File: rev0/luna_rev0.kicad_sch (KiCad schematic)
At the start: 19 parts, among them J1 USB_C_Receptacle_USB2.0, J2 USB_C_Receptacle_USB2.0, J3 USB_A, J4 USB_C_Receptacle_USB2.0, J7 PMOD_A, J8 PMOD_B, SW1 BTN_DFU, SW2 BTN_RESET, SW3 BTN_BTN

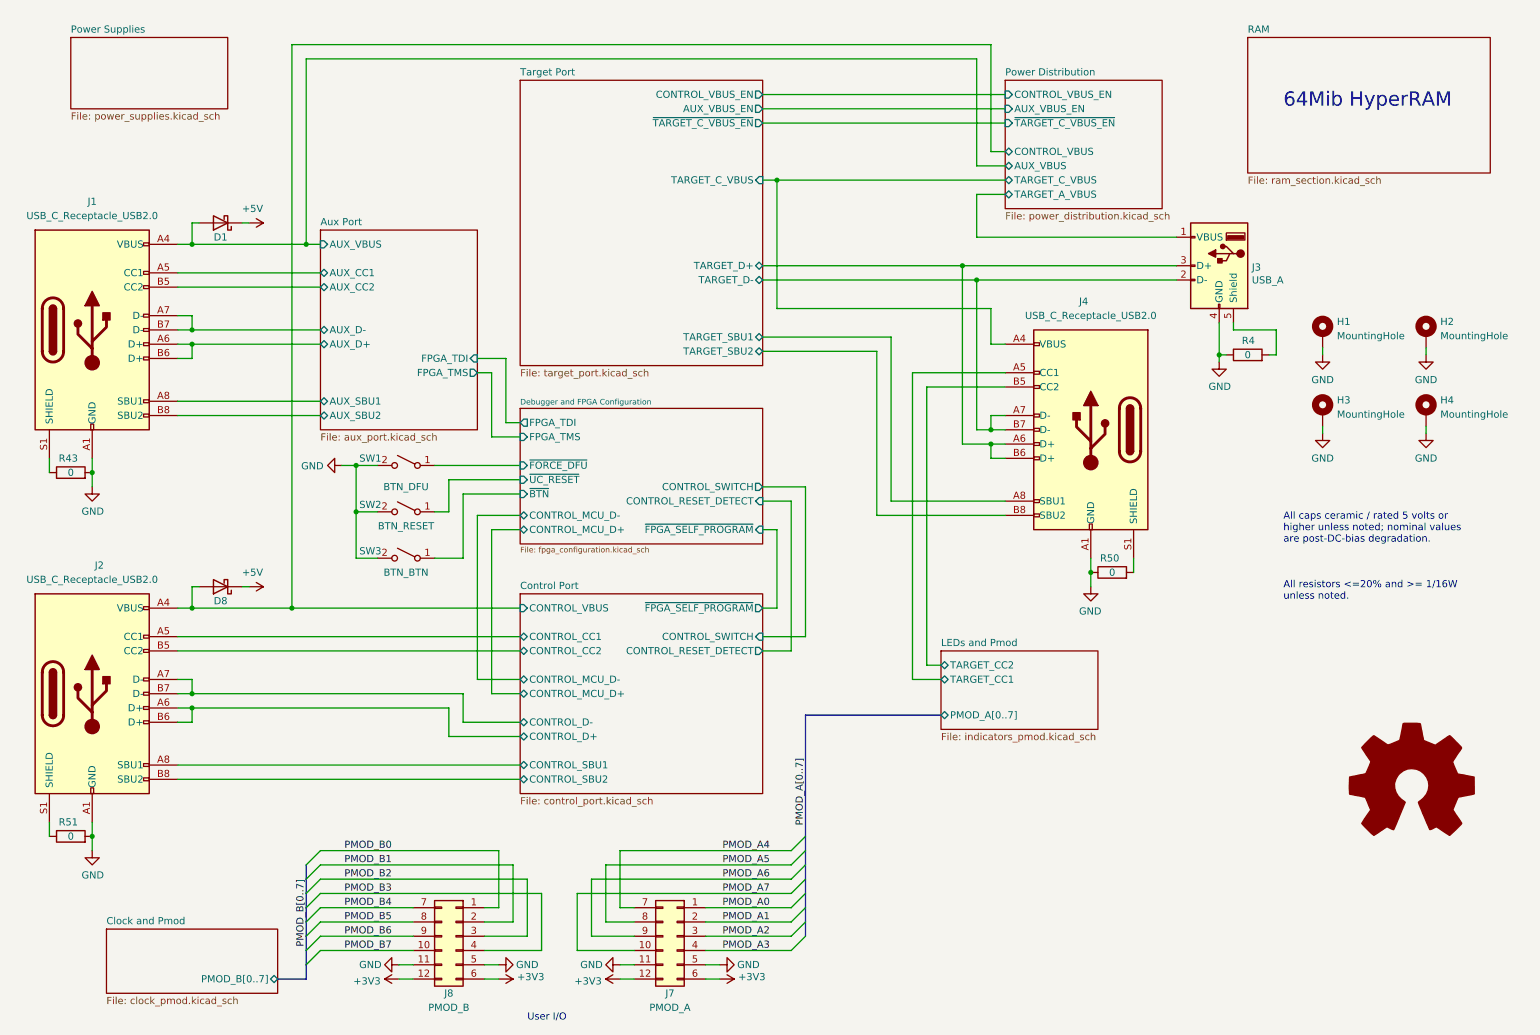
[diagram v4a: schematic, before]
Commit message: hardware: replace power input diodes
- provide input selection capability with FETs
- reduce reverse leakage current
- provide overvoltage protection
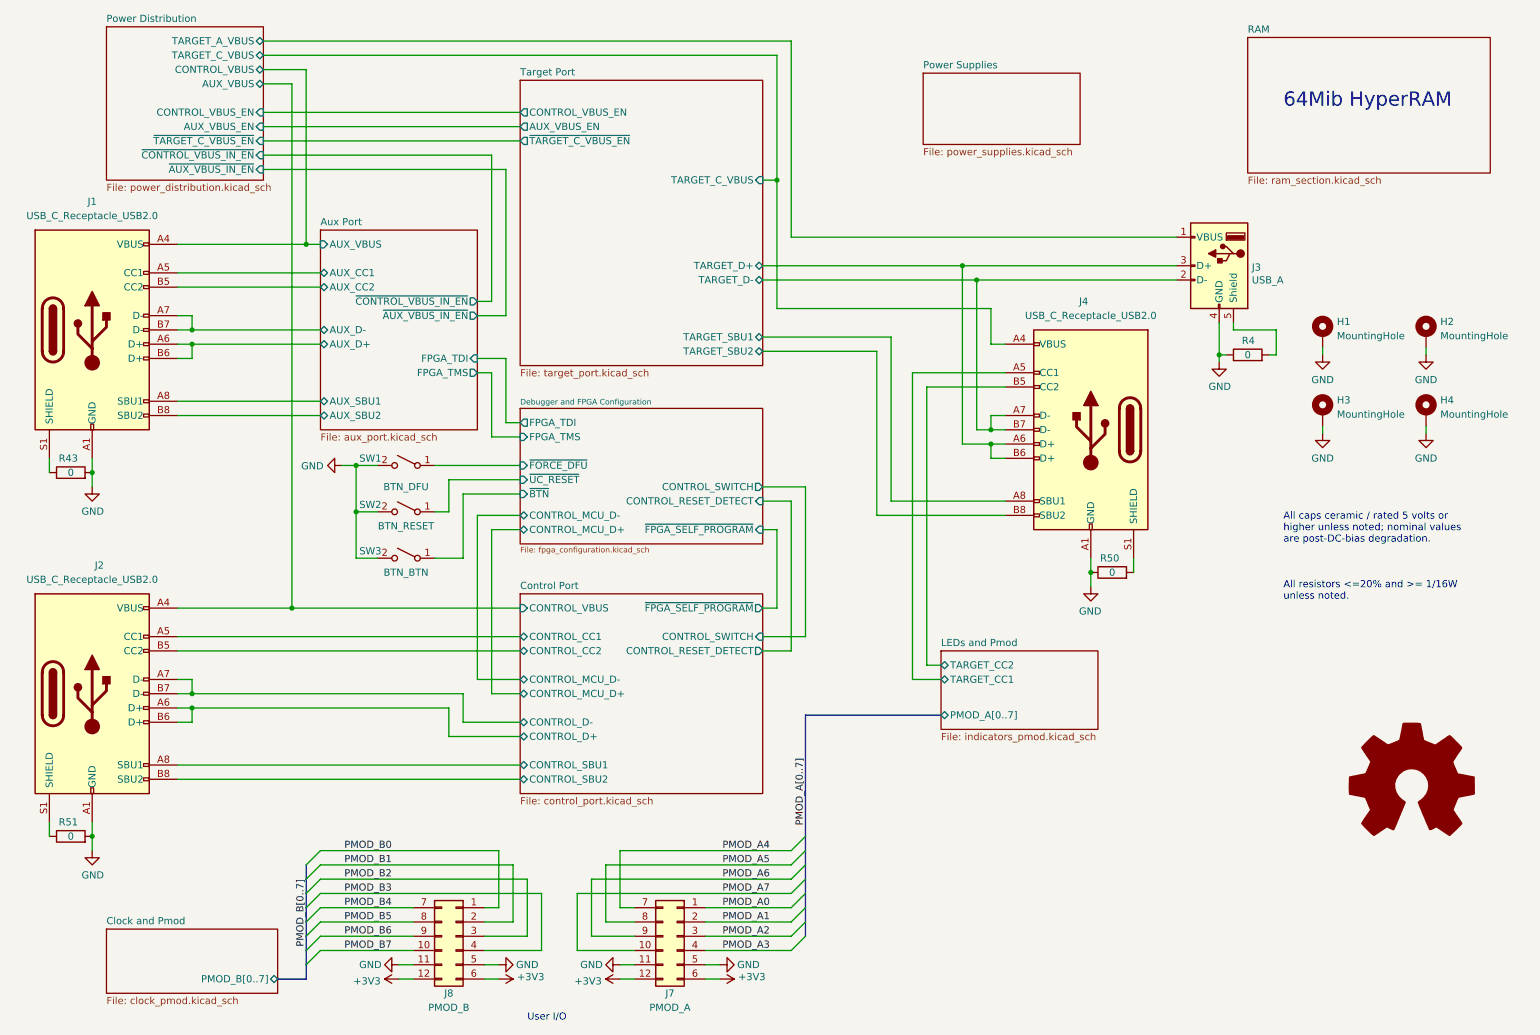
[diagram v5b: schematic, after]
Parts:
- removed D1, D8: PMEG3050BEP,115, luna:SOD128, symbol Device:D_Schottky
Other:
- sheet Aux Port ports: added ~{AUX_VBUS_IN_EN}, ~{CONTROL_VBUS_IN_EN}; removed none
- sheet Power Distribution ports: added ~{AUX_VBUS_IN_EN}, ~{CONTROL_VBUS_IN_EN}; removed none

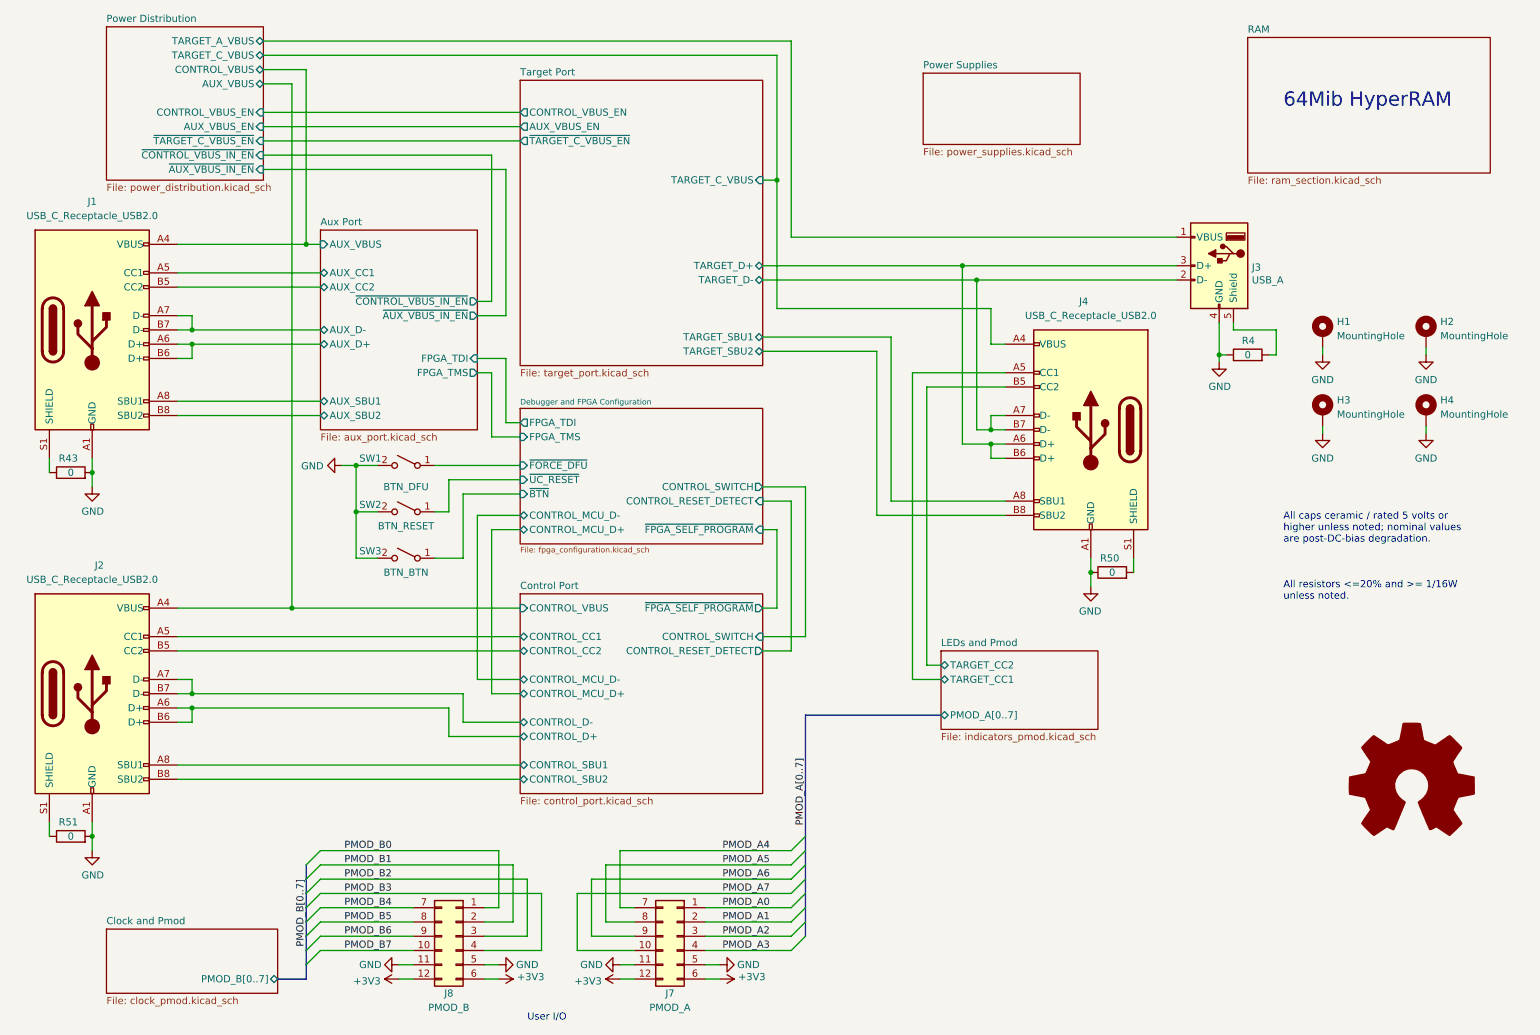
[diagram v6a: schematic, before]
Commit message: hardware: add VBUS voltage and current monitoring
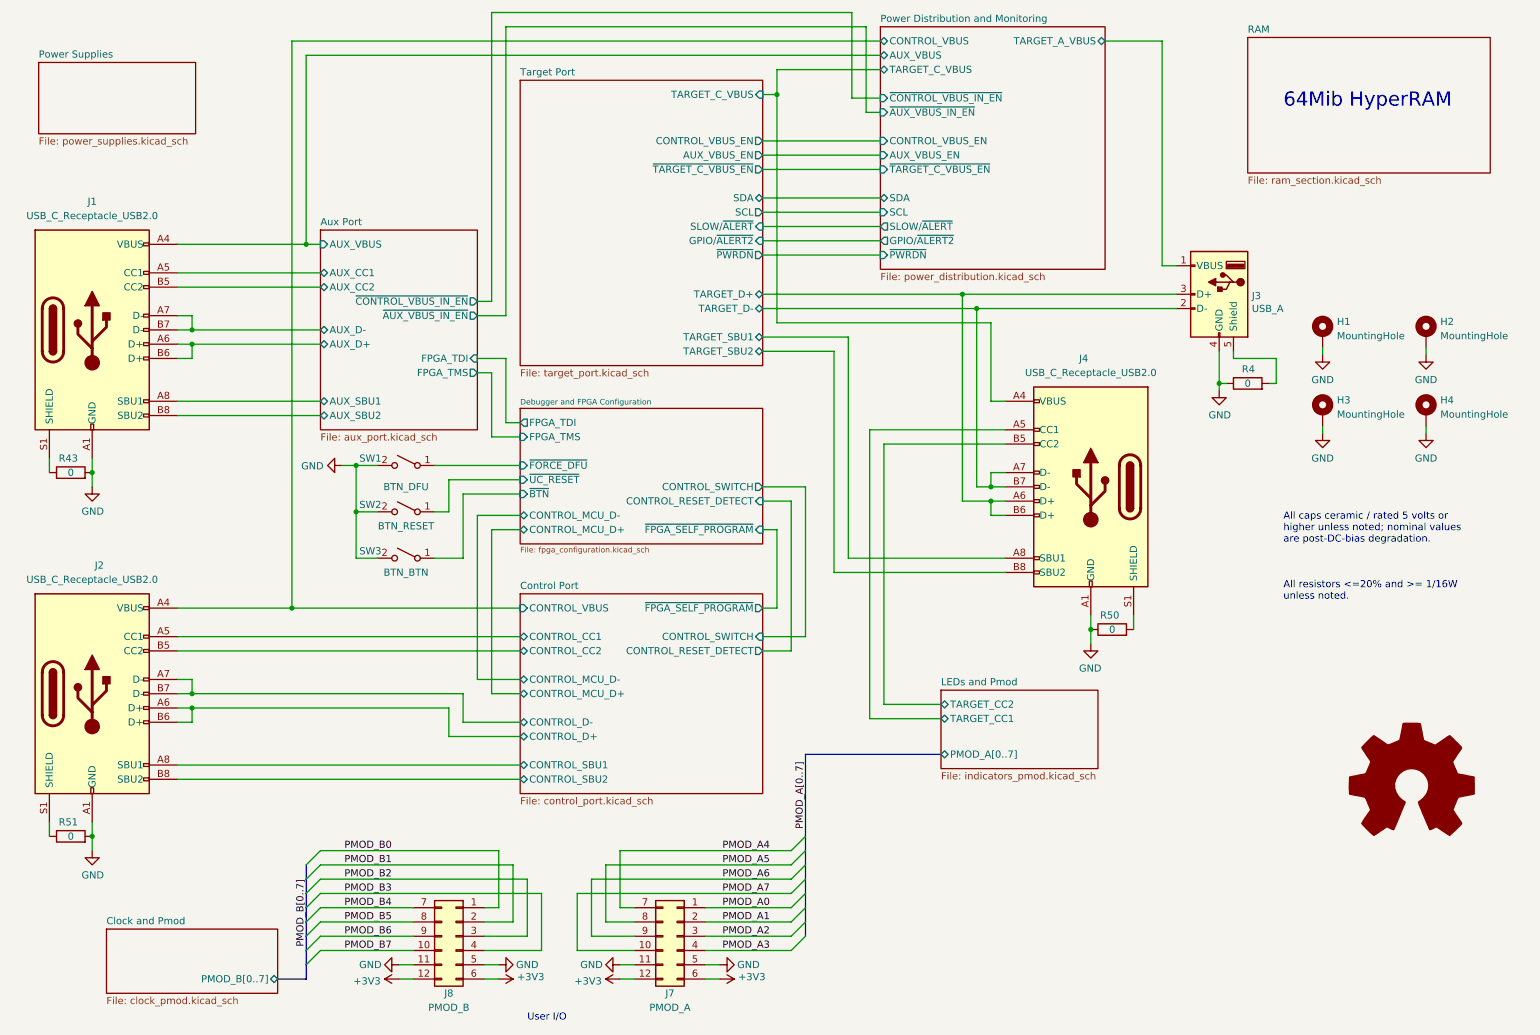
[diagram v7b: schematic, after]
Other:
- sheet Power Distribution renamed Power Distribution and Monitoring
- sheet Power Distribution and Monitoring ports: added GPIO/~{ALERT2}, SCL, SDA, SLOW/~{ALERT}, ~{PWRDN}; removed none
- sheet Target Port ports: added GPIO/~{ALERT2}, SCL, SDA, SLOW/~{ALERT}, ~{PWRDN}; removed none
- moved on the sheet: J3, J4, R4, R50

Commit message: hardware: add Target port Type-C controller
replaces buffers for CC pin I/O
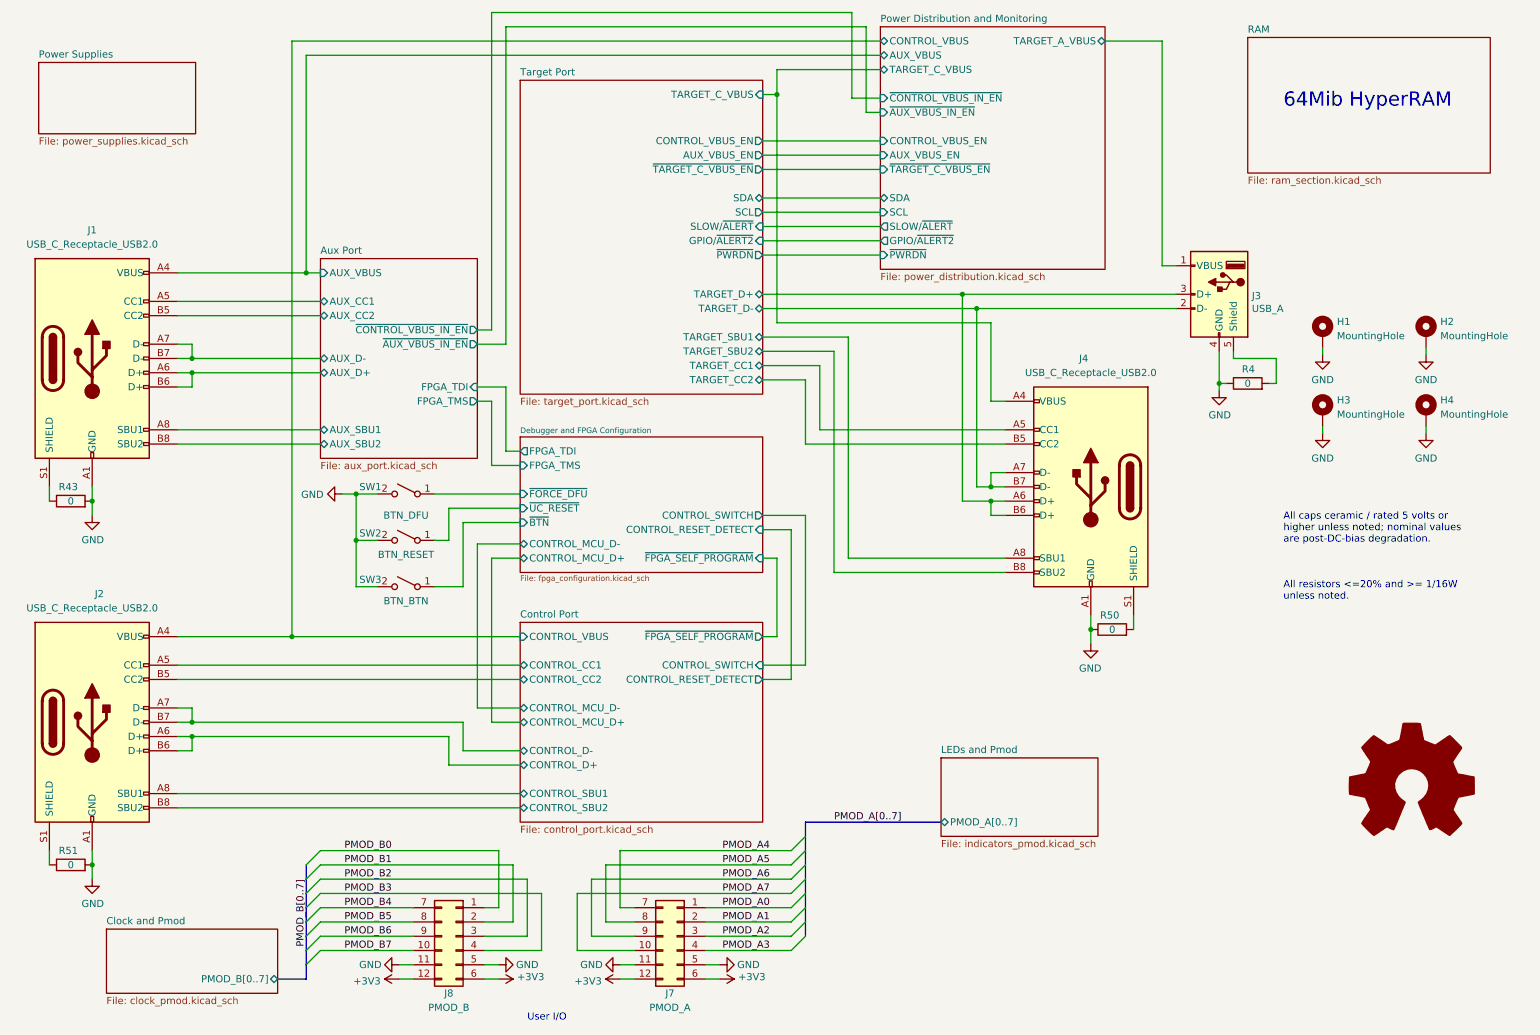
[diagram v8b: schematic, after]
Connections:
- net LEDs and Pmod/TARGET_CC1 renamed Target Port/TARGET_CC1
- net LEDs and Pmod/TARGET_CC2 renamed Target Port/TARGET_CC2
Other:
- sheet LEDs and Pmod ports: added none; removed TARGET_CC1, TARGET_CC2
- sheet Target Port ports: added TARGET_CC1, TARGET_CC2; removed none
- moved on the sheet: J1, J2, R43, R51, SW1, SW2, SW3
